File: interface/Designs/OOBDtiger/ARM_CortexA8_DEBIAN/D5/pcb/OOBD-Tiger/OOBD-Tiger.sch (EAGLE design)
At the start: 116 parts, among them IC1 ADM3053M, IC2 ADM3053M, IC4 DS3231, U1 SY6280, U10 MP1482DS, U2 SN65HVD230(SO8), U3 SY6280, U6 SN65HVD230(SO8)

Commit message: start rearranging the position of the components
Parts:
- C1, C47: device rcl:C-EU075-032X103 -> rcl:C-EUC0603K
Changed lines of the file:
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@@
 <part name="R41" library="rcl" deviceset="R-EU_" device="R0603" value="10k"/>
 <part name="V52" library="supply2" deviceset="VCC" device="" value="3.3V"/>
-<part name="C47" library="rcl" deviceset="C-EU" device="075-032X103" value="100nF"/>
+<part name="C47" library="rcl" deviceset="C-EU" device="C0603K" value="100nF"/>
 <part name="GND98" library="supply1" deviceset="GND" device="" value=""/>
 <part name="R42" library="rcl" deviceset="R-EU_" device="R0603" value="120R"/>
@@
 <part name="R5" library="rcl" deviceset="R-EU_" device="R0603" value="10k"/>
 <part name="V2" library="supply2" deviceset="VCC" device="" value="3.3V"/>
-<part name="C1" library="rcl" deviceset="C-EU" device="075-032X103" value="100nF"/>
+<part name="C1" library="rcl" deviceset="C-EU" device="C0603K" value="100nF"/>
 <part name="GND5" library="supply1" deviceset="GND" device="" value=""/>
 <part name="R6" library="rcl" deviceset="R-EU_" device="R0603" value="120R"/>

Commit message: add latest modifications to OOBD schematics
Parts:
- removed MS-CAN: OPEN, SparkFun:JUMPER-2SMD-NO
- removed R42: 120R, rcl:R-EU_R0603
- added C33, C34: NA(10nF), resistor:C-EUC0603
- added D1, D2: PESD1CAN, Industrialberry:PESD1CAN
- added HS-CAN1: OPEN, SparkFun:JUMPER-2SMD-NO
- added R31, R32, R33: 60R, resistor:R-EU_R0603
- R6: value 120R -> 60R; device rcl:R-EU_R0603 -> resistor:R-EU_R0603
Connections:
- new net N$30: HS-CAN.1, R32.2
- new net N$32: HS-CAN1.1, R33.2
- net CAN0_H: now also D1.C2, R6.2; no longer R42.2
- net CAN0_L: now also D1.C1, HS-CAN1.2; no longer MS-CAN.1
- net CAN1_H: now also D2.C2, R31.2; no longer R6.2
- net CAN1_L: now also D2.C1, HS-CAN.2; no longer HS-CAN.1
- net GND: now also C33.2, C34.2, D1.CC, D2.CC
- net N$10: now also C34.1, R33.1, R6.1; no longer MS-CAN.2, R42.1
- net N$2: now also C33.1, R31.1, R32.1; no longer HS-CAN.2, R6.1
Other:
- moved on the sheet: C1, C47, HS-CAN, R6, U2, U6

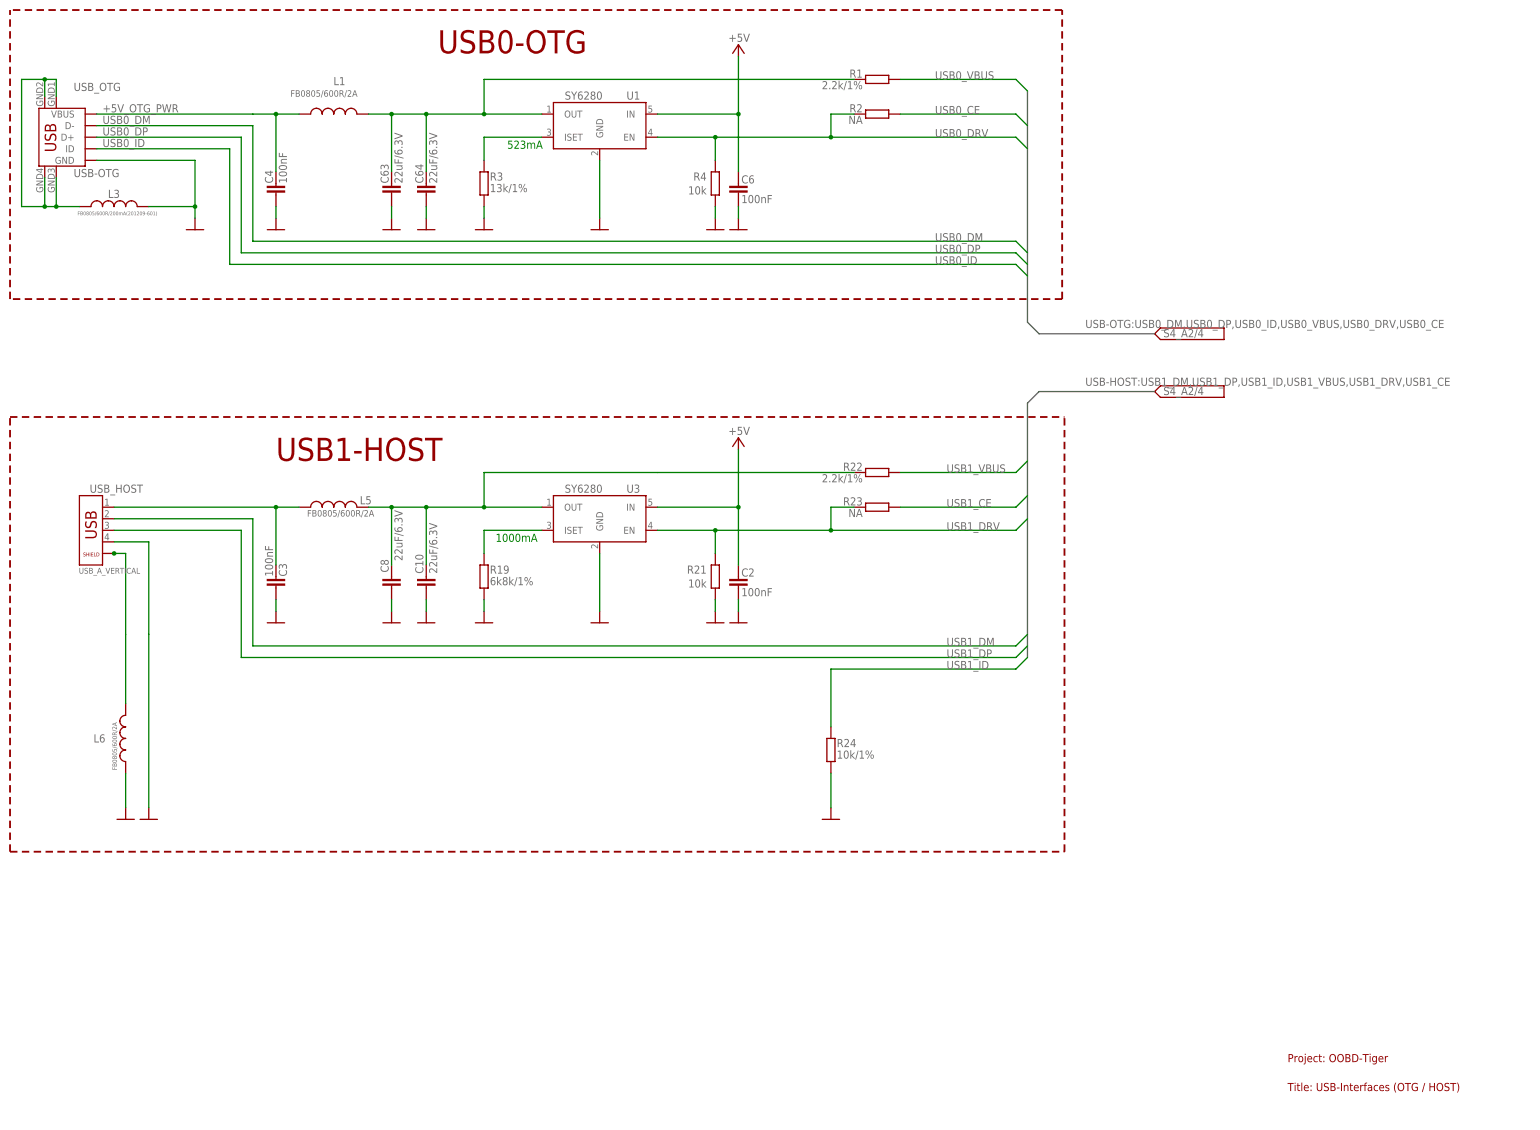
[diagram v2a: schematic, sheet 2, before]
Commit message: add OOBDpiCAN connector
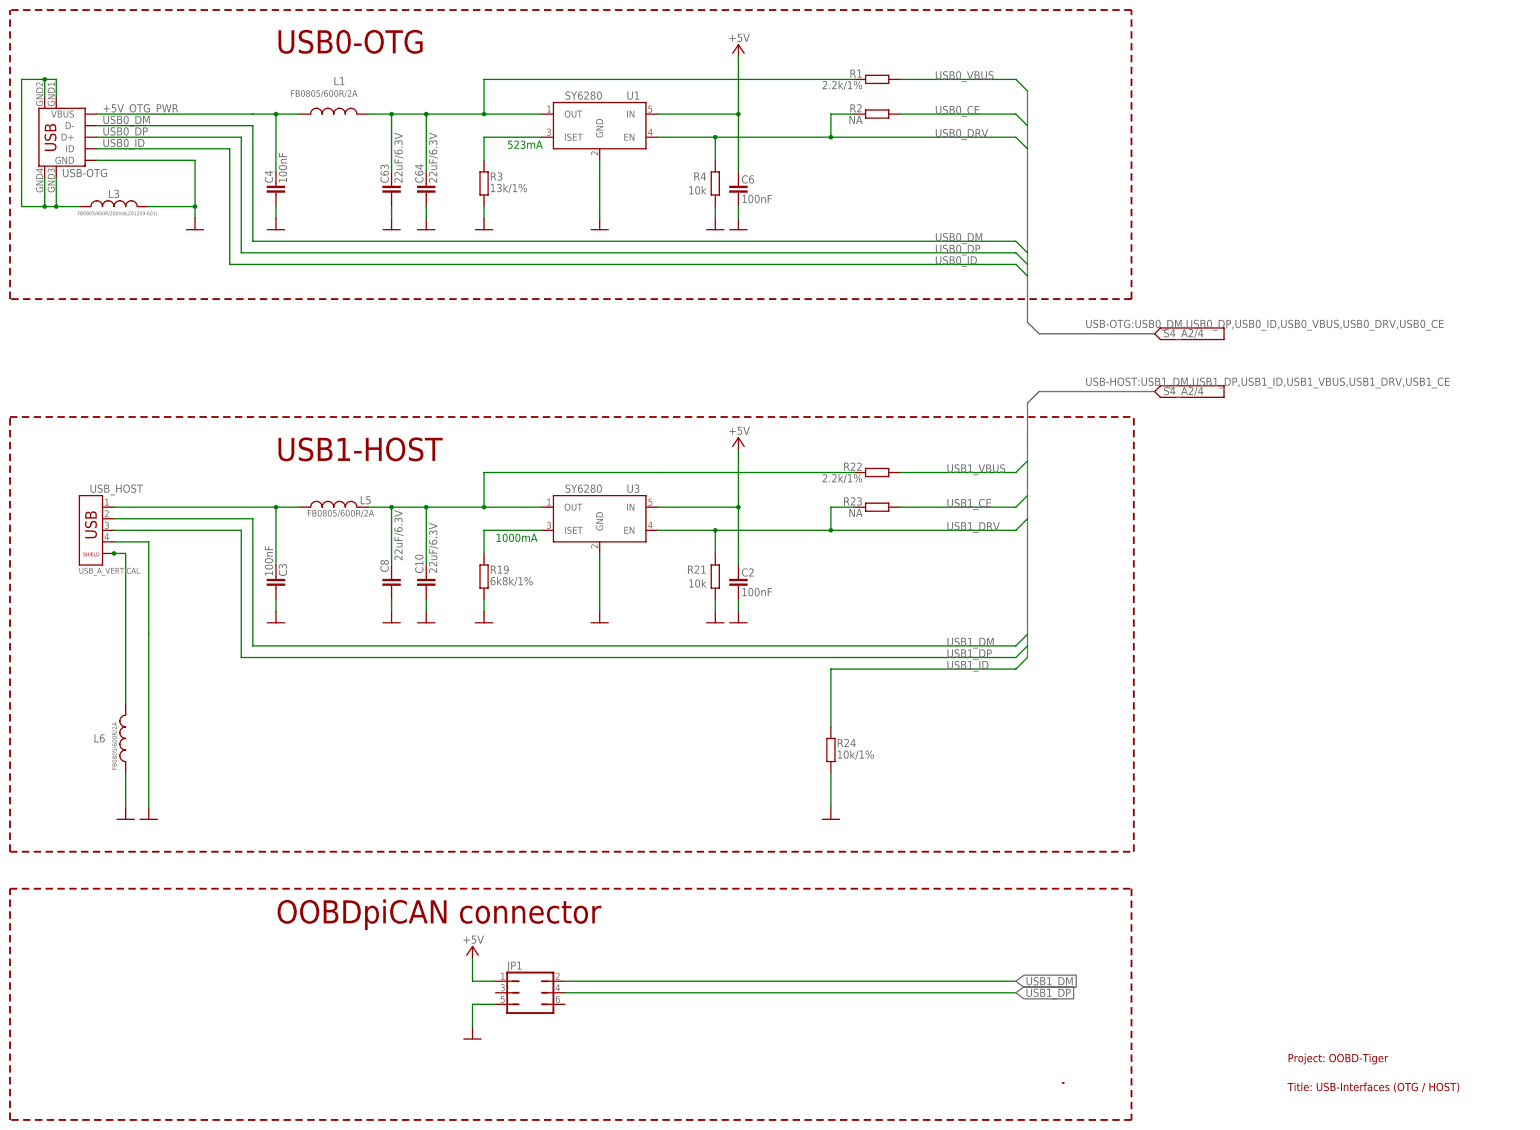
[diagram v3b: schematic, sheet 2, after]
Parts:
- added JP1: (no value), jumper:JP3Q
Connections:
- net +5V: now also JP1.1
- net GND: now also JP1.5
- net USB1_DM: now also JP1.2
- net USB1_DP: now also JP1.4
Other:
- note added: "OOBDpiCAN connector"
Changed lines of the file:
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@@
 <setting verticaltext="up"/>
 </settings>
-<grid distance="0.1" unitdist="inch" unit="mil" style="lines" multiple="1" display="yes" altdistance="0.01" altunitdist="inch" altunit="inch"/>
+<grid distance="0.1" unitdist="inch" unit="inch" style="lines" multiple="1" display="yes" altdistance="0.01" altunitdist="inch" altunit="inch"/>
 <layers>
 <layer number="1" name="Top" color="4" fill="1" visible="no" active="no"/>
@@
 <part name="GND54" library="supply1" deviceset="GND" device="" value=""/>
 <part name="GND55" library="supply1" deviceset="GND" device="" value=""/>
+<part name="JP1" library="jumper" deviceset="JP3Q" device=""/>
+<part name="GND57" library="supply1" deviceset="GND" device="" value=""/>
+<part name="P+9" library="supply1" deviceset="+5V" device=""/>
 </parts>
 <sheets>
@@
 <plain>
 <wire x1="10.16" y1="187.96" x2="10.16" y2="251.46" width="0.4064" layer="94" style="longdash"/>
-<wire x1="241.3" y1="251.46" x2="10.16" y2="251.46" width="0.4064" layer="94" style="longdash"/>
-<wire x1="241.3" y1="187.96" x2="241.3" y2="251.46" width="0.4064" layer="94" style="longdash"/>
-<wire x1="241.3" y1="187.96" x2="10.16" y2="187.96" width="0.4064" layer="94" style="longdash"/>
-<text x="104.14" y="241.935" size="5.08" layer="94">USB0-OTG</text>
+<wire x1="256.54" y1="251.46" x2="10.16" y2="251.46" width="0.4064" layer="94" style="longdash"/>
+<wire x1="256.54" y1="187.96" x2="256.54" y2="251.46" width="0.4064" layer="94" style="longdash"/>
+<wire x1="256.54" y1="187.96" x2="10.16" y2="187.96" width="0.4064" layer="94" style="longdash"/>
+<text x="68.58" y="241.935" size="5.08" layer="94">USB0-OTG</text>
 <text x="130.175" y="214.63" size="1.778" layer="214">Iset = 6800/Rs</text>
 <text x="130.175" y="210.82" size="1.778" layer="214">Iset = 523mA</text>
@@
 <text x="290.83" y="20.32" size="1.778" layer="94">Project: OOBD-Tiger</text>
 <text x="290.83" y="13.97" size="1.778" layer="94">Title: USB-Interfaces (OTG / HOST)</text>
-<wire x1="10.16" y1="66.548" x2="241.808" y2="66.548" width="0.4064" layer="94" style="longdash"/>
-<wire x1="10.16" y1="162.052" x2="241.808" y2="162.052" width="0.4064" layer="94" style="longdash"/>
+<wire x1="10.16" y1="66.548" x2="257.048" y2="66.548" width="0.4064" layer="94" style="longdash"/>
+<wire x1="10.16" y1="162.052" x2="257.048" y2="162.052" width="0.4064" layer="94" style="longdash"/>
 <wire x1="10.16" y1="66.548" x2="10.16" y2="162.052" width="0.4064" layer="94" style="longdash"/>
-<wire x1="241.808" y1="66.548" x2="241.808" y2="162.052" width="0.4064" layer="94" style="longdash"/>
+<wire x1="257.048" y1="66.548" x2="257.048" y2="162.052" width="0.4064" layer="94" style="longdash"/>
 <text x="68.58" y="152.4" size="5.08" layer="94">USB1-HOST</text>
 <text x="119.38" y="220.98" size="1.778" layer="91">523mA</text>
 <text x="116.84" y="134.62" size="1.778" layer="91">1000mA</text>
+<wire x1="241.3" y1="15.748" x2="241.808" y2="15.748" width="0.4064" layer="94" style="longdash"/>
+<wire x1="10.16" y1="58.42" x2="256.54" y2="58.42" width="0.4064" layer="94" style="longdash"/>
+<wire x1="256.54" y1="58.42" x2="256.54" y2="7.62" width="0.4064" layer="94" style="longdash"/>
+<wire x1="256.54" y1="7.62" x2="10.16" y2="7.62" width="0.4064" layer="94" style="longdash"/>
+<wire x1="10.16" y1="7.62" x2="10.16" y2="58.42" width="0.4064" layer="94" style="longdash"/>
+<text x="68.58" y="50.8" size="5.08" layer="94">OOBDpiCAN connector</text>
 </plain>
 <instances>
@@
 </instance>
 <instance part="USB_OTG" gate="G1" x="24.13" y="224.79" smashed="yes" rot="MR0">
-<attribute name="NAME" x="24.13" y="233.68" size="1.778" layer="95"/>
-<attribute name="VALUE" x="24.13" y="216.535" size="1.778" layer="96" rot="MR180"/>
+<attribute name="VALUE" x="21.59" y="216.535" size="1.778" layer="96" rot="MR180"/>
 </instance>
 <instance part="R1" gate="G$1" x="200.66" y="236.22" smashed="yes" rot="MR0">
@@
 <instance part="GND32" gate="1" x="190.5" y="73.66" rot="MR0"/>
 <instance part="SUPPLY8" gate="G$1" x="276.86" y="167.64"/>
+<instance part="JP1" gate="B" x="124.46" y="35.56" rot="R270"/>
+<instance part="GND57" gate="1" x="111.76" y="25.4" rot="MR0"/>
+<instance part="P+9" gate="1" x="111.76" y="45.72" smashed="yes" rot="MR0">
+<attribute name="VALUE" x="114.3" y="46.355" size="1.778" layer="96" rot="MR0"/>
+</instance>
 </instances>
 <busses>
@@
 <wire x1="139.7" y1="132.08" x2="139.7" y2="119.38" width="0.1524" layer="91"/>
 </segment>
+<segment>
+<pinref part="JP1" gate="B" pin="5"/>
+<pinref part="GND57" gate="1" pin="GND"/>
+<wire x1="116.84" y1="33.02" x2="111.76" y2="33.02" width="0.1524" layer="91"/>
+<wire x1="111.76" y1="33.02" x2="111.76" y2="27.94" width="0.1524" layer="91"/>
+</segment>
 </net>
 <net name="+5V" class="0">
@@
 <pinref part="P+1" gate="1" pin="+5V"/>
 <pinref part="U3" gate="G$1" pin="IN"/>
+</segment>
+<segment>
+<pinref part="JP1" gate="B" pin="1"/>
+<pinref part="P+9" gate="1" pin="+5V"/>
+<wire x1="116.84" y1="38.1" x2="111.76" y2="38.1" width="0.1524" layer="91"/>
+<wire x1="111.76" y1="38.1" x2="111.76" y2="43.18" width="0.1524" layer="91"/>
 </segment>
 </net>
@@
 <label x="215.9" y="111.76" size="1.778" layer="95"/>
 </segment>
+<segment>
+<pinref part="JP1" gate="B" pin="2"/>
+<wire x1="132.08" y1="38.1" x2="231.14" y2="38.1" width="0.1524" layer="91"/>
+<label x="231.14" y="38.1" size="1.778" layer="95" xref="yes"/>
+</segment>
 </net>
 <net name="USB1_DP" class="0">
@@
 <label x="215.9" y="109.22" size="1.778" layer="95"/>
 </segment>
-</net>
+<segment>
+<pinref part="JP1" gate="B" pin="4"/>
+<wire x1="132.08" y1="35.56" x2="231.14" y2="35.56" width="0.1524" layer="91"/>
+<label x="231.14" y="35.56" size="1.778" layer="95" xref="yes"/>
+</segment>
+</net>
